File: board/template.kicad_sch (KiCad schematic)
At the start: 10 parts, among them J1 USB4081-03-A, Q1 NTTFS5C673NLTAG, Q2 NTTFS5C673NLTAG, U1 APK43070DKZ-13-FA01

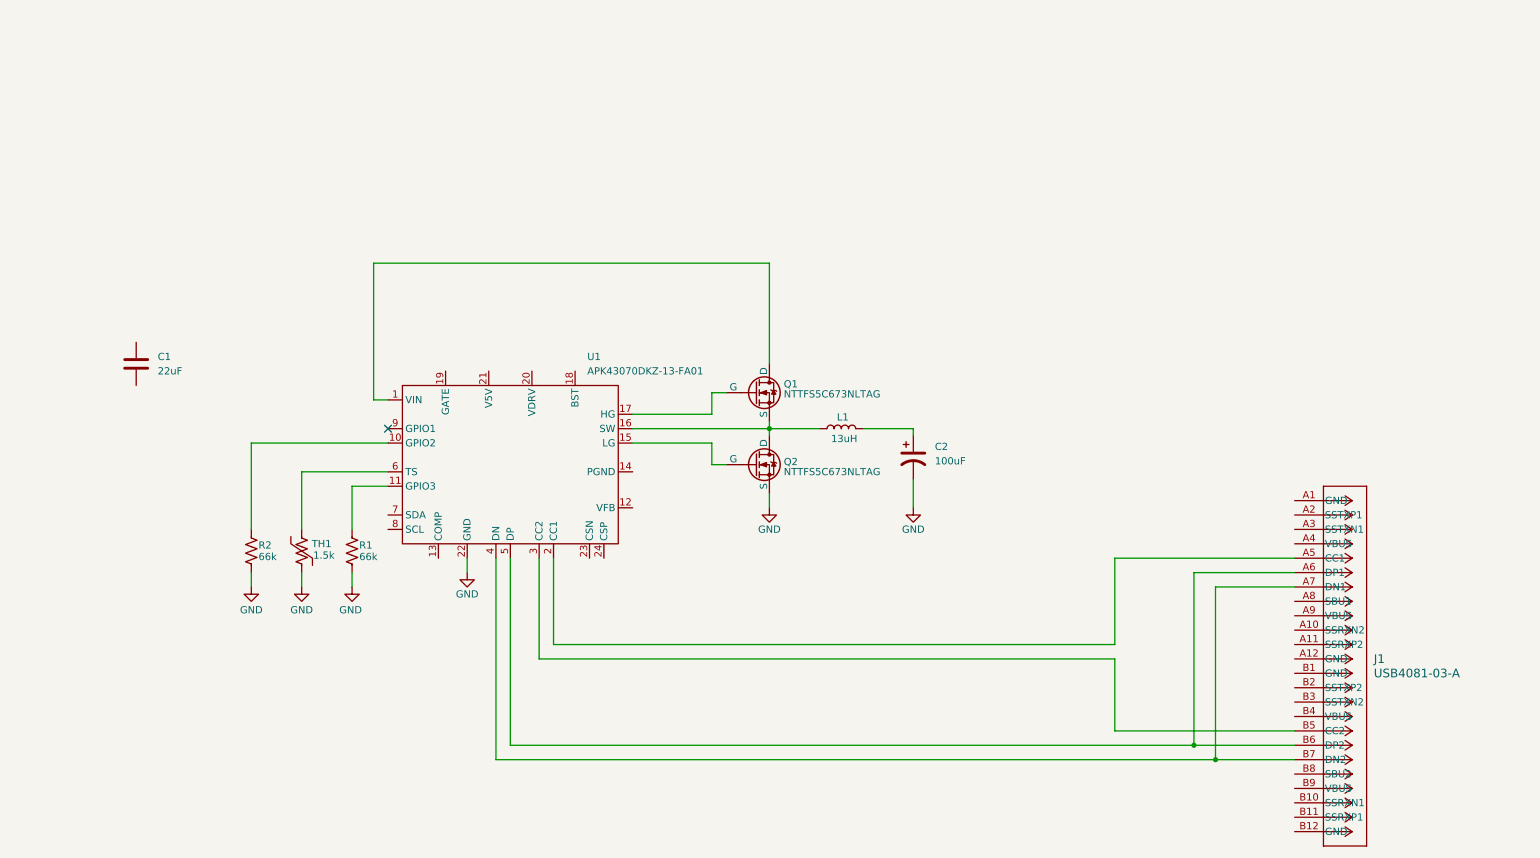
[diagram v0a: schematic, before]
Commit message: Added compensation network
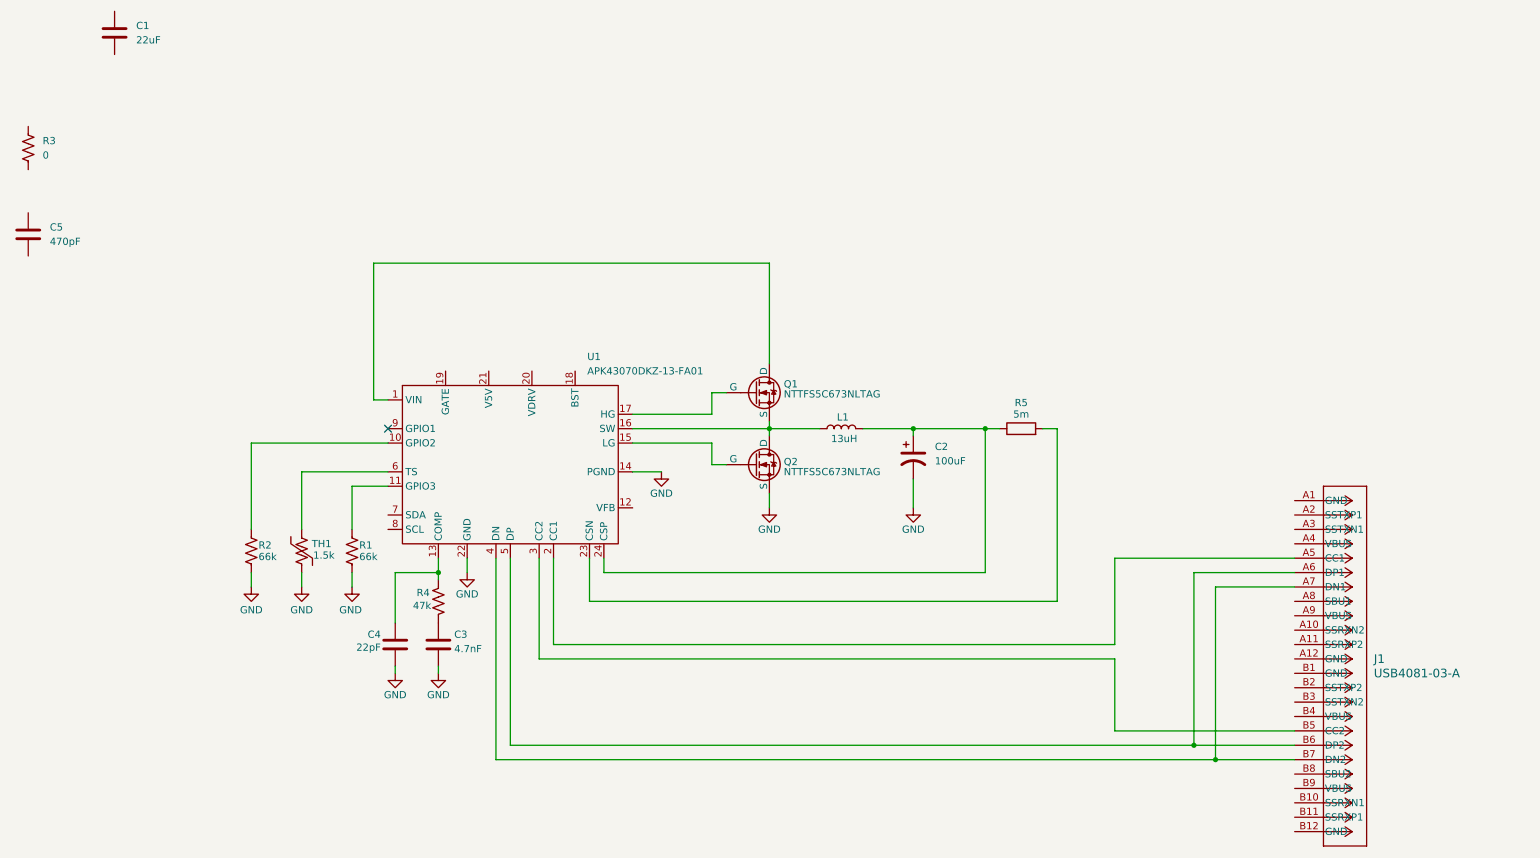
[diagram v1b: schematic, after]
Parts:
- added C3: 4.7nF, symbol Device:C
- added C4: 22pF, symbol Device:C
- added C5: 470pF, symbol Device:C
- added R3: 0, symbol Device:R_US
- added R4: 47k, symbol Device:R_US
- added R5: 5m, symbol Device:R
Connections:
- net GND: now also U1.14 (PGND), C3.2, C4.2
- net at U1.13 (COMP): now also C4.1, R4.1
- net at U1.23 (CSN): now also R5.2
- net at U1.24 (CSP): now also C2.1, L1.2, R5.1
- new net: C3.1, R4.2
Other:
- moved on the sheet: C1

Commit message: Finished connecting pins of main IC
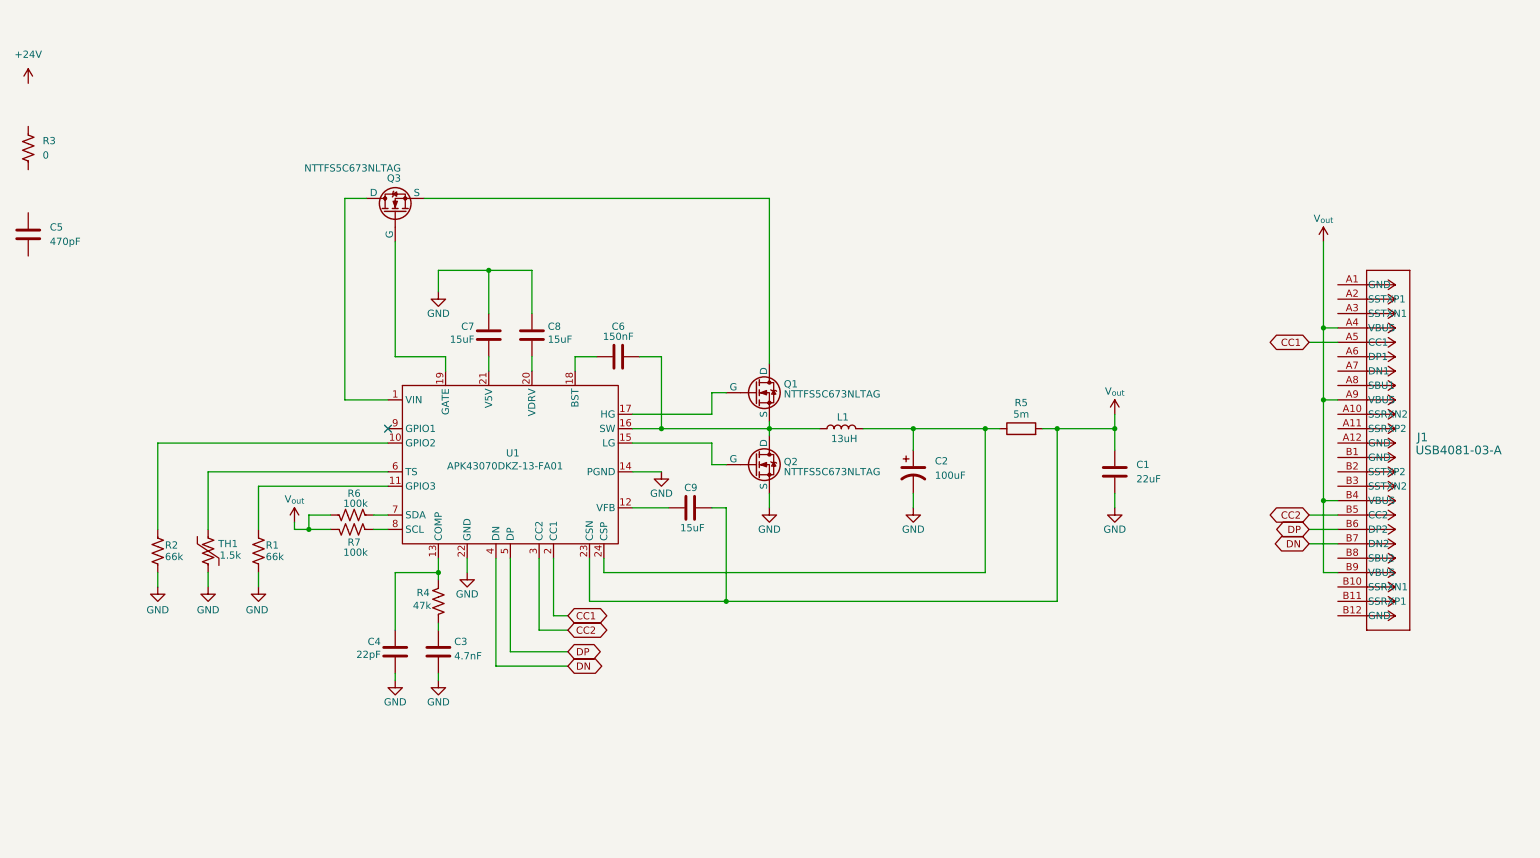
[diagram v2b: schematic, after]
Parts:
- added C6: 150nF, symbol Device:C
- added C7, C8, C9: 15uF, symbol Device:C
- added Q3: NTTFS5C673NLTAG, symbol Simulation_SPICE:NMOS
- added R6, R7: 100k, symbol Device:R_US
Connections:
- net GND: now also C1.2, C7.2, C8.1
- net at Q1.1 (D): now also Q3.3 (S); no longer U1.1 (VIN)
- net at L1.1, Q1.3 (S), Q2.1 (D)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: now also C6.1
- net at U1.12 (VFB): now also C9.1
- net at U1.18 (BST): now also C6.2
- net at U1.19 (GATE): now also Q3.2 (G)
- net CC1: now reaches J1.A5 (CC1), U1.2 (CC1)
- net at U1.20 (VDRV): now also C8.2
- net at U1.21 (V5V): now also C7.1
- net V_{out}: now reaches R5.2, U1.23 (CSN)
- net V_{out}: now also C1.1, J1.A4 (VBUS), J1.A9 (VBUS), J1.B4 (VBUS), J1.B9 (VBUS), C9.2, R6.1, R7.1
- net CC2: now reaches J1.B5 (CC2), U1.3 (CC2)
- net DN: now reaches J1.B7 (DN2), U1.4 (DN)
- net DN: no longer J1.A7 (DN1)
- net DP: now reaches J1.B6 (DP2), U1.5 (DP)
- net DP: no longer J1.A6 (DP1)
- net at U1.7 (SDA): now also R6.2
- net at U1.8 (SCL): now also R7.2
- new net: Q3.1 (D), U1.1 (VIN)
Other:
- moved on the sheet: C1, C2, C3, C4, J1, R1, R2, TH1

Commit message: Fixed compensation loop
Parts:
- removed C9: 15uF, symbol Device:C
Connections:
- net V_{out}: now also R3.2
- net V_{batt}: now reaches Q3.1 (D), U1.1 (VIN)
- net at U1.12 (VFB): now also C5.2
- net at C5.1: now also R3.1
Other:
- moved on the sheet: C5, R3
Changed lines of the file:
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@@
 	)
 	(junction
-		(at 248.92 85.09)
+		(at 76.2 49.53)
 		(diameter 0)
 		(color 0 0 0 0)
 	)
 	(junction
-		(at 143.51 120.65)
+		(at 248.92 85.09)
 		(diameter 0)
 		(color 0 0 0 0)
@@
 	)
 	(junction
+		(at 147.32 120.65)
+		(diameter 0)
+		(color 0 0 0 0)
+	)
+	(junction
 		(at 69.85 107.95)
 		(diameter 0)
@@
 	(wire
 		(pts
-			(xy 140.97 104.14) (xy 143.51 104.14)
+			(xy 138.43 104.14) (xy 139.7 104.14)
 		)
 		(stroke
@@
 	(wire
 		(pts
-			(xy 127 104.14) (xy 133.35 104.14)
+			(xy 127 104.14) (xy 130.81 104.14)
 		)
 		(stroke
@@
 	(wire
 		(pts
-			(xy 119.38 120.65) (xy 143.51 120.65)
+			(xy 119.38 120.65) (xy 147.32 120.65)
 		)
 		(stroke
@@
 	(wire
 		(pts
-			(xy 93.98 80.01) (xy 93.98 77.47)
+			(xy 147.32 120.65) (xy 201.93 120.65)
 		)
 		(stroke
@@
 	(wire
 		(pts
-			(xy 143.51 120.65) (xy 201.93 120.65)
+			(xy 93.98 80.01) (xy 93.98 77.47)
 		)
 		(stroke
@@
 	(wire
 		(pts
+			(xy 62.23 49.53) (xy 76.2 49.53)
+		)
+		(stroke
+			(width 0)
+			(type default)
+		)
+	)
+	(wire
+		(pts
 			(xy 92.71 115.57) (xy 92.71 116.84)
 		)
@@
 	(wire
 		(pts
-			(xy 127 97.79) (xy 132.08 97.79)
+			(xy 127 97.79) (xy 130.81 97.79)
 		)
 		(stroke
@@
 	(wire
 		(pts
+			(xy 62.23 49.53) (xy 62.23 48.26)
+		)
+		(stroke
+			(width 0)
+			(type default)
+		)
+	)
+	(wire
+		(pts
 			(xy 176.53 90.17) (xy 167.64 90.17)
 		)
@@
 	(wire
 		(pts
-			(xy 143.51 104.14) (xy 143.51 120.65)
+			(xy 147.32 104.14) (xy 147.32 120.65)
 		)
 		(stroke
@@
 	(symbol
 		(lib_id "Device:C")
-		(at 20.32 55.88 0)
+		(at 134.62 104.14 270)
 		(unit 1)
 		(exclude_from_sim no)
@@
 		(on_board yes)
 		(dnp no)
-		(fields_autoplaced yes)
 		(property "Reference" "C5"
-			(at 24.13 54.6099 0)
+			(at 134.62 108.204 90)
 			(effects
 				(font
 					(size 1.27 1.27)
 				)
-				(justify left)
 			)
 		)
 		(property "Value" "470pF"
-			(at 24.13 57.1499 0)
+			(at 134.62 110.49 90)
 			(effects
 				(font
 					(size 1.27 1.27)
 				)
-				(justify left)
 			)
 		)
 		(property "Footprint" ""
-			(at 21.2852 59.69 0)
+			(at 130.81 105.1052 0)
 			(effects
 				(font
@@
 		)
 		(property "Datasheet" "~"
-			(at 20.32 55.88 0)
+			(at 134.62 104.14 0)
 			(effects
 				(font
@@
 		)
 		(property "Description" "Unpolarized capacitor"
-			(at 20.32 55.88 0)
+			(at 134.62 104.14 0)
 			(effects
 				(font
@@
 	)
 	(symbol
-		(lib_id "Device:C")
-		(at 137.16 104.14 90)
-		(mirror x)
-		(unit 1)
-		(exclude_from_sim no)
-		(in_bom yes)
-		(on_board yes)
-		(dnp no)
-		(property "Reference" "C9"
-			(at 138.43 100.584 90)
-			(effects
-				(font
-					(size 1.27 1.27)
-				)
-				(justify left)
-			)
-		)
-		(property "Value" "15uF"
-			(at 139.7 107.696 90)
-			(effects
-				(font
-					(size 1.27 1.27)
-				)
-				(justify left)
-			)
-		)
-		(property "Footprint" ""
-			(at 140.97 105.1052 0)
-			(effects
-				(font
-					(size 1.27 1.27)
-				)
-				(hide yes)
-			)
-		)
-		(property "Datasheet" "https://www.digikey.com/en/products/detail/samsung-electro-mechanics/CL10X106MO8NRNC/5961253"
-			(at 137.16 104.14 0)
-			(effects
-				(font
-					(size 1.27 1.27)
-				)
-				(hide yes)
-			)
-		)
-		(property "Description" "Unpolarized capacitor"
-			(at 137.16 104.14 0)
-			(effects
-				(font
-					(size 1.27 1.27)
-				)
-				(hide yes)
-			)
-		)
-		(pin "1"
-		)
-		(pin "2"
-		)
-		(instances
-			(project "template"
-				(path "/fbd9c71c-f200-4aab-a303-9f269bc9de13"
-					(reference "C9")
-					(unit 1)
-				)
-			)
-		)
-	)
-	(symbol
 		(lib_id "Device:R_US")
 		(at 77.47 105.41 90)
@@
 	(symbol
 		(lib_id "power:+24V")
-		(at 20.32 29.21 0)
+		(at 62.23 48.26 0)
 		(unit 1)
 		(exclude_from_sim no)
@@
 		(fields_autoplaced yes)
 		(property "Reference" "#PWR011"
-			(at 20.32 33.02 0)
+			(at 62.23 52.07 0)
 			(effects
 				(font
@@
 			)
 		)
-		(property "Value" "+24V"
-			(at 20.32 24.13 0)
+		(property "Value" "V_{batt}"
+			(at 62.23 43.18 0)
 			(effects
 				(font
@@
 		)
 		(property "Footprint" ""
-			(at 20.32 29.21 0)
+			(at 62.23 48.26 0)
 			(effects
 				(font
@@
 		)
 		(property "Datasheet" ""
-			(at 20.32 29.21 0)
+			(at 62.23 48.26 0)
 			(effects
 				(font
@@
 		)
 		(property "Description" "Power symbol creates a global label with name \"+24V\""
-			(at 20.32 29.21 0)
+			(at 62.23 48.26 0)
 			(effects
 				(font
@@
 	(symbol
 		(lib_id "power:GND")
-		(at 132.08 97.79 0)
+		(at 130.81 97.79 0)
 		(unit 1)
 		(exclude_from_sim no)
@@
 		(dnp no)
 		(property "Reference" "#PWR09"
-			(at 132.08 104.14 0)
+			(at 130.81 104.14 0)
 			(effects
 				(font
@@
 		)
 		(property "Value" "GND"
-			(at 132.08 101.6 0)
+			(at 130.81 101.6 0)
 			(effects
 				(font
@@
 		)
 		(property "Footprint" ""
-			(at 132.08 97.79 0)
+			(at 130.81 97.79 0)
 			(effects
 				(font
@@
 		)
 		(property "Datasheet" ""
-			(at 132.08 97.79 0)
+			(at 130.81 97.79 0)
 			(effects
 				(font
@@
 		)
 		(property "Description" "Power symbol creates a global label with name \"GND\" , ground"
-			(at 132.08 97.79 0)
+			(at 130.81 97.79 0)
 			(effects
 				(font
@@
 	(symbol
 		(lib_id "Device:R_US")
-		(at 20.32 40.64 0)
+		(at 143.51 104.14 90)
+		(mirror x)
 		(unit 1)
 		(exclude_from_sim no)
@@
 		(on_board yes)
 		(dnp no)
-		(fields_autoplaced yes)
 		(property "Reference" "R3"
-			(at 22.86 39.3699 0)
+			(at 143.51 106.68 90)
 			(effects
 				(font
 					(size 1.27 1.27)
 				)
-				(justify left)
 			)
 		)
 		(property "Value" "0"
-			(at 22.86 41.9099 0)
+			(at 143.51 108.712 90)
 			(effects
 				(font
 					(size 1.27 1.27)
 				)
-				(justify left)
 			)
 		)
 		(property "Footprint" ""
-			(at 21.336 40.894 90)
+			(at 143.764 105.156 90)
 			(effects
 				(font
@@
 		)
 		(property "Datasheet" "~"
-			(at 20.32 40.64 0)
+			(at 143.51 104.14 0)
 			(effects
 				(font
@@
 		)
 		(property "Description" "Resistor, US symbol"
-			(at 20.32 40.64 0)
+			(at 143.51 104.14 0)
 			(effects
 				(font
